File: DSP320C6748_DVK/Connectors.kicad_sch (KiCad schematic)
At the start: 10 parts, among them J13 Conn_02x25_Odd_Even, J14 525593652, J15 Conn_02x25_Odd_Even, J16 Conn_02x10_Odd_Even, J17 Conn_02x10_Odd_Even, J18 Conn_01x02_Pin, J19 Conn_01x02_Pin, J20 Conn_01x02_Pin

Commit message: Whole Schematic Reannotation Done
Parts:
- renumbered J16 to J14, J17 to J15, J15 to J16, J14 to J17, J20 to J18, J18 to J19, J19 to J20, R253 to R223, R254 to R224

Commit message: Schematic Corrections-II Done
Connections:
- net +1V8D: now also J15.2 (Pin_2); no longer J15.1 (Pin_1)
- net 5V_{IN}: now also J16.46 (Pin_46)
- net AIC_BCLK: now also J16.41 (Pin_41); no longer J16.39 (Pin_39)
- net AIC_MCLK: now also J16.39 (Pin_39); no longer J16.37 (Pin_37)
- net AIC_WCLK: now also J16.37 (Pin_37); no longer J16.41 (Pin_41)
- net AXR_{15}: now also J16.36 (Pin_36); no longer J16.32 (Pin_32)
- net AXR_{8}: now also J16.32 (Pin_32); no longer J16.36 (Pin_36)
- net GND: no longer J16.46 (Pin_46)
- net LCD_1V8_D_0: now also J14.5 (Pin_5); no longer J14.6 (Pin_6)
- net LCD_1V8_D_1: now also J14.8 (Pin_8); no longer J14.7 (Pin_7)
- net LCD_1V8_D_10: now also J15.13 (Pin_13), J15.7 (Pin_7); no longer J15.14 (Pin_14), J15.8 (Pin_8)
- net LCD_1V8_D_11: now also J14.13 (Pin_13); no longer J14.14 (Pin_14)
- net LCD_1V8_D_12: now also J15.3 (Pin_3); no longer J15.4 (Pin_4)
- net LCD_1V8_D_13: now also J15.4 (Pin_4), J15.8 (Pin_8); no longer J15.3 (Pin_3), J15.7 (Pin_7)
- net LCD_1V8_D_14: now also J14.14 (Pin_14), J15.5 (Pin_5); no longer J14.13 (Pin_13), J15.6 (Pin_6)
- net LCD_1V8_D_15: now also J14.11 (Pin_11), J15.6 (Pin_6); no longer J14.12 (Pin_12), J15.5 (Pin_5)
- net LCD_1V8_D_2: now also J14.4 (Pin_4), J14.7 (Pin_7); no longer J14.3 (Pin_3), J14.8 (Pin_8)
- net LCD_1V8_D_3: now also J14.3 (Pin_3), J15.15 (Pin_15); no longer J14.4 (Pin_4), J15.16 (Pin_16)
- net LCD_1V8_D_4: now also J14.6 (Pin_6), J15.9 (Pin_9); no longer J14.5 (Pin_5), J15.10 (Pin_10)
- net LCD_1V8_D_5: now also J14.10 (Pin_10); no longer J14.9 (Pin_9)
- net LCD_1V8_D_6: now also J14.16 (Pin_16); no longer J14.15 (Pin_15)
- net LCD_1V8_D_7: now also J14.9 (Pin_9); no longer J14.10 (Pin_10)
- net LCD_1V8_D_8: now also J15.10 (Pin_10); no longer J15.9 (Pin_9)
- net LCD_1V8_D_9: now also J14.12 (Pin_12), J15.11 (Pin_11); no longer J14.11 (Pin_11), J15.12 (Pin_12)
- net LCD_AC_ENB_~{CS}_1V8: now also J15.17 (Pin_17); no longer J15.18 (Pin_18)
- net LCD_HSYNC_1V8: now also J15.18 (Pin_18); no longer J15.17 (Pin_17)
- net LCD_PCLK_1V8: now also J15.16 (Pin_16); no longer J15.15 (Pin_15)
- net LCD_SCL: now also J15.14 (Pin_14); no longer J15.13 (Pin_13)
- net LCD_SDA: now also J14.15 (Pin_15); no longer J14.16 (Pin_16)
- net LCD_VSYNC_1V8: now also J14.17 (Pin_17); no longer J14.18 (Pin_18)
- net TS_INT: now also J15.12 (Pin_12); no longer J15.11 (Pin_11)
- net ~{PHP_RST}: now also J14.18 (Pin_18); no longer J14.17 (Pin_17)
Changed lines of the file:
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@@
 	(global_label "AIC_WCLK"
 		(shape input)
-		(at 116.84 81.28 180)
+		(at 116.84 76.2 180)
 		(fields_autoplaced yes)
 		(effects
@@
 		)
 		(property "Intersheetrefs" "${INTERSHEET_REFS}"
-			(at 104.9043 81.28 0)
+			(at 104.9043 76.2 0)
 			(hide yes)
 			(show_name no)
@@
 	(global_label "AXR_{8}"
 		(shape input)
-		(at 140.97 73.66 0)
+		(at 140.97 68.58 0)
 		(effects
 			(font
@@
 		)
 		(property "Intersheetrefs" "${INTERSHEET_REFS}"
-			(at 140.97 73.66 0)
+			(at 140.97 68.58 0)
 			(hide yes)
 			(show_name no)
@@
 	(global_label "AIC_MCLK"
 		(shape input)
-		(at 116.84 76.2 180)
+		(at 116.84 78.74 180)
 		(fields_autoplaced yes)
 		(effects
@@
 		)
 		(property "Intersheetrefs" "${INTERSHEET_REFS}"
-			(at 104.9043 76.2 0)
+			(at 104.9043 78.74 0)
 			(hide yes)
 			(show_name no)
@@
 	(global_label "AIC_BCLK"
 		(shape input)
-		(at 116.84 78.74 180)
+		(at 116.84 81.28 180)
 		(fields_autoplaced yes)
 		(effects
@@
 		)
 		(property "Intersheetrefs" "${INTERSHEET_REFS}"
-			(at 105.0857 78.74 0)
+			(at 105.0857 81.28 0)
 			(hide yes)
 			(show_name no)
@@
 	(global_label "AXR_{15}"
 		(shape input)
-		(at 140.97 68.58 0)
+		(at 140.97 73.66 0)
 		(effects
 			(font
@@
 		)
 		(property "Intersheetrefs" "${INTERSHEET_REFS}"
-			(at 140.97 68.58 0)
+			(at 140.97 73.66 0)
 			(hide yes)
 			(show_name no)
@@
 		)
 	)
+	(global_label "5V_{IN}"
+		(shape input)
+		(at 134.62 88.9 0)
+		(fields_autoplaced yes)
+		(effects
+			(font
+				(size 1.27 1.27)
+				(thickness 0.254)
+				(bold yes)
+			)
+			(justify left)
+		)
+		(property "Intersheetrefs" "${INTERSHEET_REFS}"
+			(at 141.9783 88.9 0)
+			(hide yes)
+			(show_name no)
+			(do_not_autoplace no)
+			(effects
+				(font
+					(size 1.27 1.27)
+				)
+				(justify left)
+			)
+		)
+	)
 	(global_label "EMA_A_5"
 		(shape bidirectional)
@@
 	(symbol
 		(lib_id "Connector_Generic:Conn_02x10_Odd_Even")
-		(at 111.76 140.97 0)
+		(at 114.3 140.97 0)
+		(mirror y)
 		(unit 1)
 		(body_style 1)
@@
 		(in_pos_files yes)
 		(dnp no)
-		(fields_autoplaced yes)
 		(property "Reference" "J15"
 			(at 113.03 124.46 0)
@@
 		)
 		(property "Footprint" ""
-			(at 111.76 140.97 0)
+			(at 114.3 140.97 0)
 			(hide yes)
 			(show_name no)
@@
 		)
 		(property "Datasheet" ""
-			(at 111.76 140.97 0)
+			(at 114.3 140.97 0)
 			(hide yes)
 			(show_name no)
@@
 		)
 		(property "Description" "Generic connector, double row, 02x10, odd/even pin numbering scheme (row 1 odd numbers, row 2 even numbers), script generated (kicad-library-utils/schlib/autogen/connector/)"
-			(at 111.76 140.97 0)
+			(at 114.3 140.97 0)
 			(hide yes)
 			(show_name no)
@@
 	)
 	(symbol
-		(lib_id "power:GND")
-		(at 134.62 88.9 0)
-		(unit 1)
-		(body_style 1)
-		(exclude_from_sim no)
-		(in_bom yes)
-		(on_board yes)
-		(in_pos_files yes)
-		(dnp no)
-		(property "Reference" "#PWR0356"
-			(at 134.62 95.25 0)
-			(hide yes)
-			(show_name no)
-			(do_not_autoplace no)
-			(effects
-				(font
-					(size 1.27 1.27)
-				)
-			)
-		)
-		(property "Value" "GND"
-			(at 134.62 92.456 0)
-			(show_name no)
-			(do_not_autoplace no)
-			(effects
-				(font
-					(size 1.27 1.27)
-				)
-			)
-		)
-		(property "Footprint" ""
-			(at 134.62 88.9 0)
-			(hide yes)
-			(show_name no)
-			(do_not_autoplace no)
-			(effects
-				(font
-					(size 1.27 1.27)
-				)
-			)
-		)
-		(property "Datasheet" ""
-			(at 134.62 88.9 0)
-			(hide yes)
-			(show_name no)
-			(do_not_autoplace no)
-			(effects
-				(font
-					(size 1.27 1.27)
-				)
-			)
-		)
-		(property "Description" "Power symbol creates a global label with name \"GND\" , ground"
-			(at 134.62 88.9 0)
-			(hide yes)
-			(show_name no)
-			(do_not_autoplace no)
-			(effects
-				(font
-					(size 1.27 1.27)
-				)
-			)
-		)
-		(pin "1"
-		)
-		(instances
-			(project "DSP320C6748_DVK"
-				(path "/3a70ffc0-9fe7-4a5b-b3c2-23140355df82/5c92834a-e218-4842-9f37-78ba42443e32"
-					(reference "#PWR0356")
-					(unit 1)
-				)
-			)
-		)
-	)
-	(symbol
 		(lib_id "525593652:525593652")
 		(at 171.45 39.37 90)
@@
 	(symbol
 		(lib_id "Connector_Generic:Conn_02x10_Odd_Even")
-		(at 53.34 142.24 0)
+		(at 55.88 142.24 0)
+		(mirror y)
 		(unit 1)
 		(body_style 1)
@@
 		(in_pos_files yes)
 		(dnp no)
-		(fields_autoplaced yes)
 		(property "Reference" "J14"
 			(at 54.61 125.73 0)
@@
 		)
 		(property "Footprint" ""
-			(at 53.34 142.24 0)
+			(at 55.88 142.24 0)
 			(hide yes)
 			(show_name no)
@@
 		)
 		(property "Datasheet" ""
-			(at 53.34 142.24 0)
+			(at 55.88 142.24 0)
 			(hide yes)
 			(show_name no)
@@
 		)
 		(property "Description" "Generic connector, double row, 02x10, odd/even pin numbering scheme (row 1 odd numbers, row 2 even numbers), script generated (kicad-library-utils/schlib/autogen/connector/)"
-			(at 53.34 142.24 0)
+			(at 55.88 142.24 0)
 			(hide yes)
 			(show_name no)

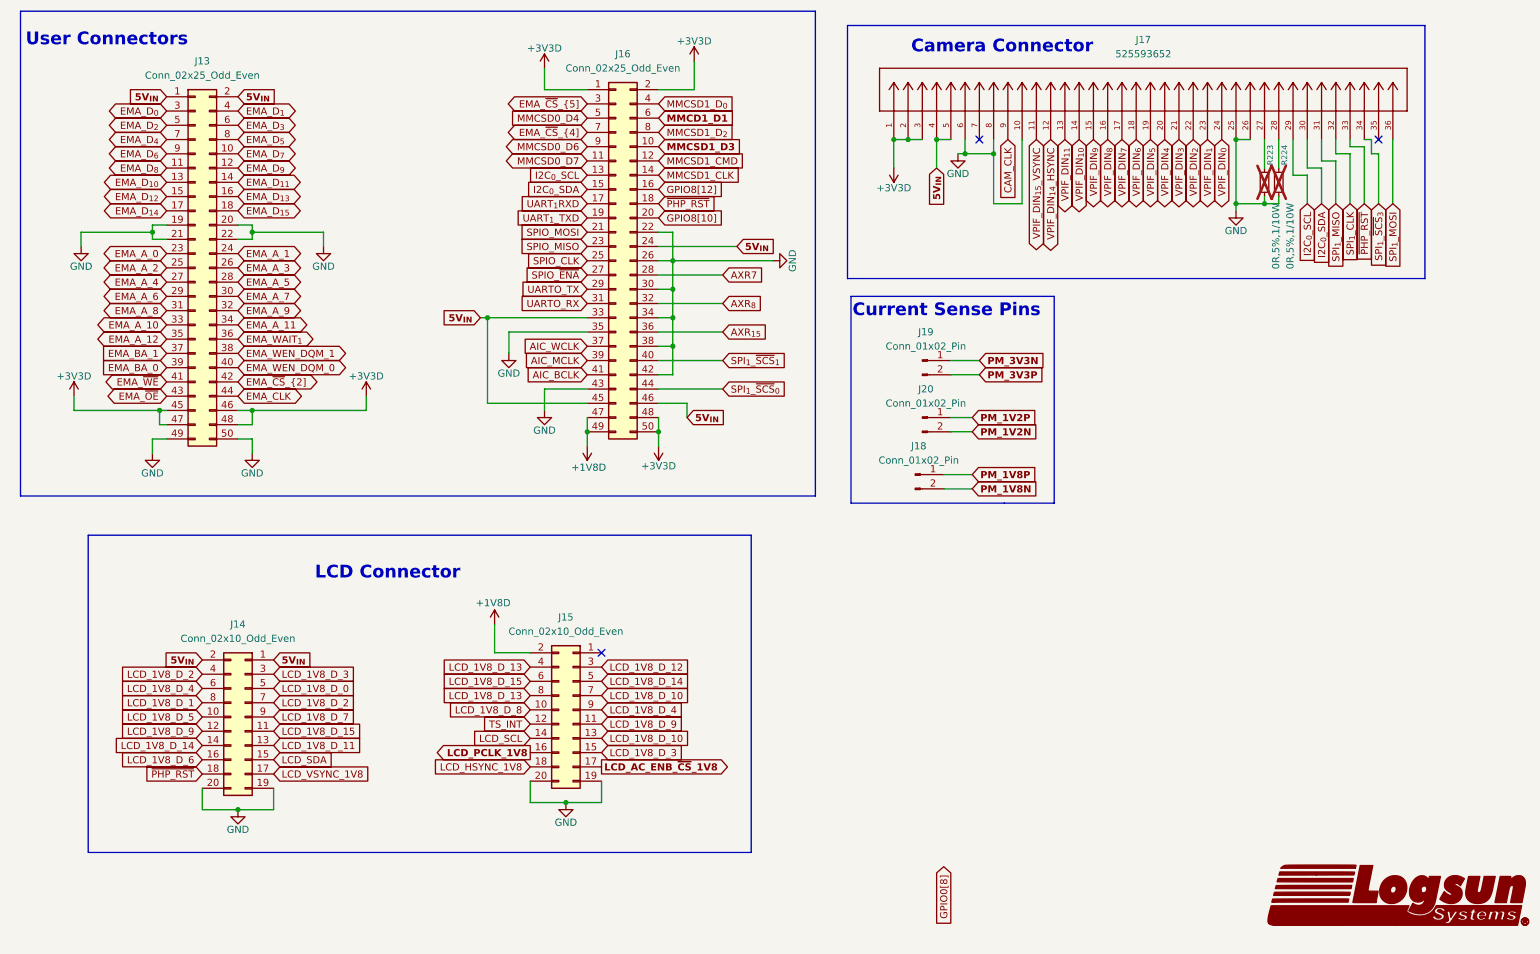
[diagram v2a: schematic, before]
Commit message: DC jack Replaced With Type-C, ADC and RTC section added
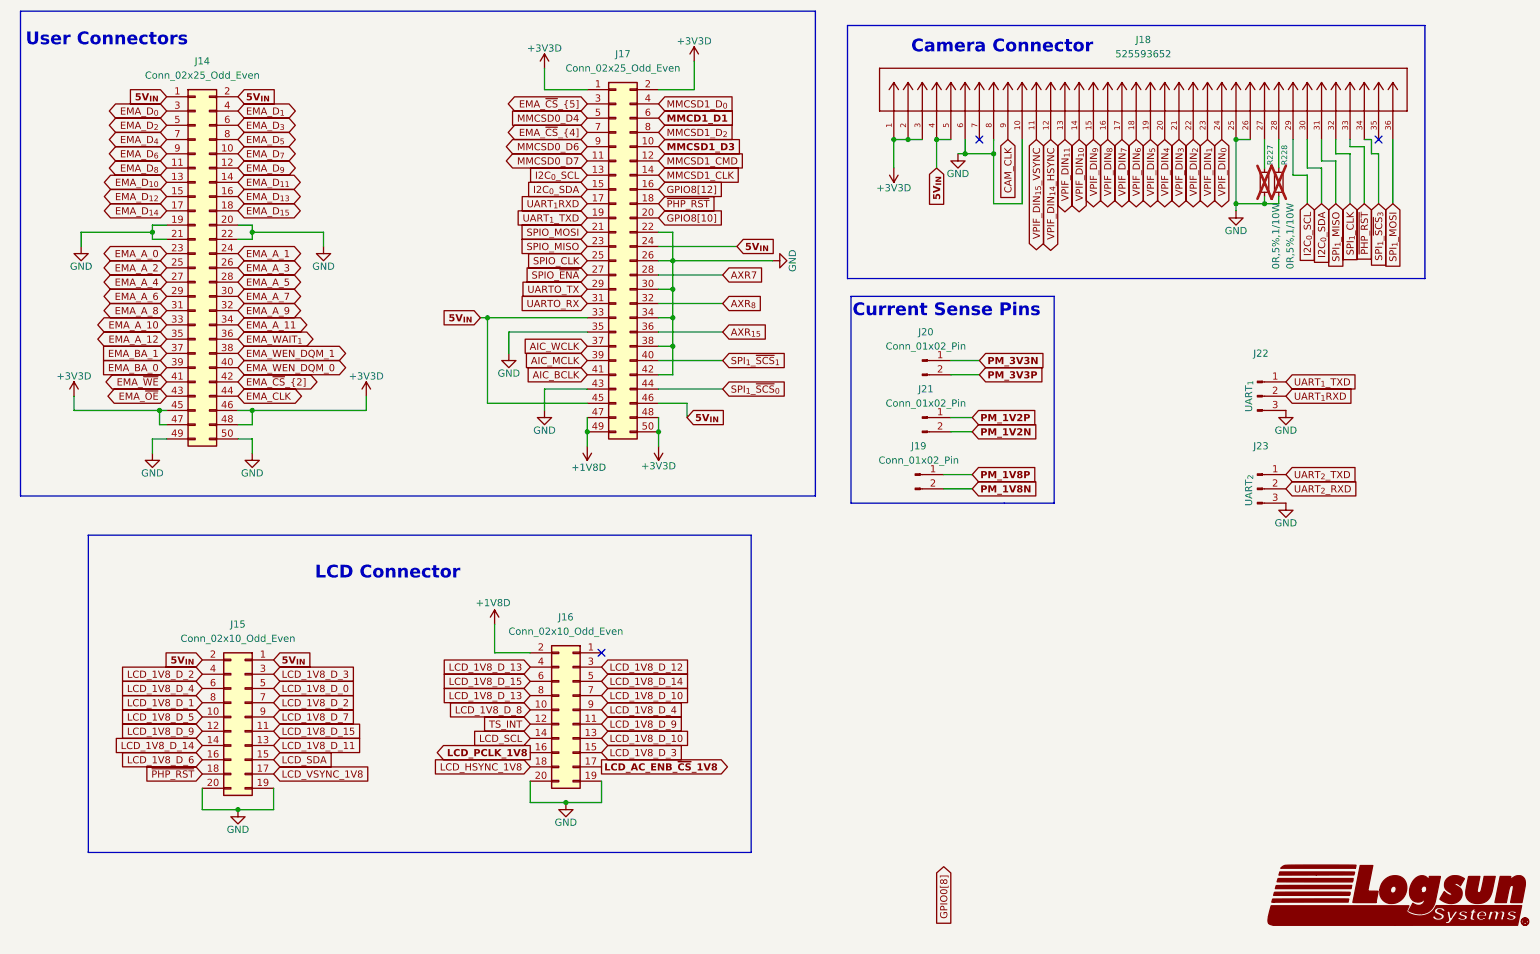
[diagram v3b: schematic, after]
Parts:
- added J22: UART_{1}, symbol Connector:Conn_01x03_Pin
- added J23: UART_{2}, symbol Connector:Conn_01x03_Pin
- renumbered J13 to J14, J14 to J15, J15 to J16, J16 to J17, J17 to J18, J18 to J19, J19 to J20, J20 to J21, R223 to R227, R224 to R228
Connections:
- net GND: now also J22.3 (Pin_3), J23.3 (Pin_3)
- net UART_{1}RXD: now also J22.2 (Pin_2)
- net UART_{1}_TXD: now also J22.1 (Pin_1)
- new net UART_{2}_RXD: J23.2 (Pin_2)
- new net UART_{2}_TXD: J23.1 (Pin_1)
